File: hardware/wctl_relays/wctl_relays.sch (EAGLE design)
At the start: 38 parts, among them IC1 74LS595D

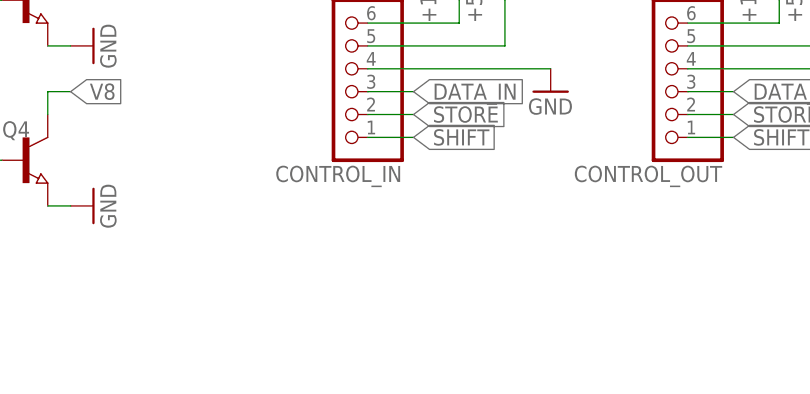
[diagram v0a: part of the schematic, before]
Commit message: Migrated back to ESP32, updated pins in code and updated hardware, also updated readme
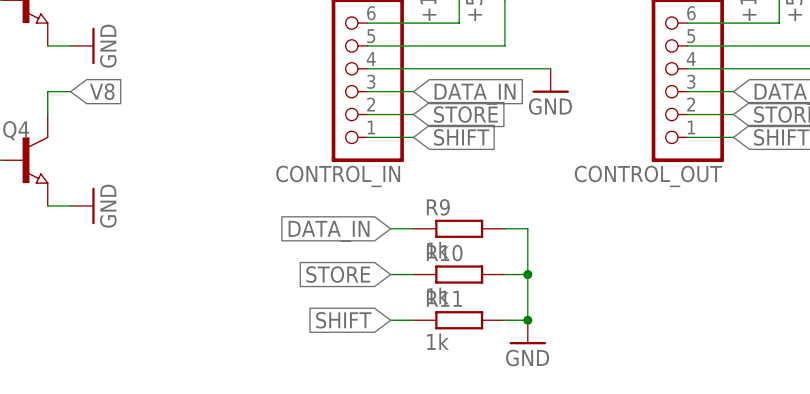
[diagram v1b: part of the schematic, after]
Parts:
- added R10, R11, R9: 1k, rcl:R-EU_R0603
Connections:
- net DATA_IN: now also R9.1
- net GND: now also R10.2, R11.2, R9.2
- net SHIFT: now also R11.1
- net STORE: now also R10.1
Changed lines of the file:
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@@
 <part name="P+6" library="supply1" library_urn="urn:adsk.eagle:library:371" deviceset="+12V" device=""/>
 <part name="P+7" library="supply1" library_urn="urn:adsk.eagle:library:371" deviceset="+5V" device=""/>
+<part name="R9" library="rcl" library_urn="urn:adsk.eagle:library:334" deviceset="R-EU_" device="R0603" package3d_urn="urn:adsk.eagle:package:23555/3" value="1k"/>
+<part name="R10" library="rcl" library_urn="urn:adsk.eagle:library:334" deviceset="R-EU_" device="R0603" package3d_urn="urn:adsk.eagle:package:23555/3" value="1k"/>
+<part name="R11" library="rcl" library_urn="urn:adsk.eagle:library:334" deviceset="R-EU_" device="R0603" package3d_urn="urn:adsk.eagle:package:23555/3" value="1k"/>
+<part name="GND13" library="supply1" library_urn="urn:adsk.eagle:library:371" deviceset="GND" device=""/>
 </parts>
 <sheets>
@@
 <instance part="P+7" gate="1" x="50.8" y="12.7" smashed="yes" grouprefs="CONTROL_IO">
 <attribute name="VALUE" x="48.26" y="7.62" size="1.778" layer="96" rot="R90"/>
+</instance>
+<instance part="R9" gate="G$1" x="10.16" y="-15.24" smashed="yes" grouprefs="CONTROL_IO">
+<attribute name="NAME" x="6.35" y="-13.7414" size="1.778" layer="95"/>
+<attribute name="VALUE" x="6.35" y="-18.542" size="1.778" layer="96"/>
+</instance>
+<instance part="R10" gate="G$1" x="10.16" y="-20.32" smashed="yes" grouprefs="CONTROL_IO">
+<attribute name="NAME" x="6.35" y="-18.8214" size="1.778" layer="95"/>
+<attribute name="VALUE" x="6.35" y="-23.622" size="1.778" layer="96"/>
+</instance>
+<instance part="R11" gate="G$1" x="10.16" y="-25.4" smashed="yes" grouprefs="CONTROL_IO">
+<attribute name="NAME" x="6.35" y="-23.9014" size="1.778" layer="95"/>
+<attribute name="VALUE" x="6.35" y="-28.702" size="1.778" layer="96"/>
+</instance>
+<instance part="GND13" gate="1" x="17.78" y="-27.94" smashed="yes" grouprefs="CONTROL_IO">
+<attribute name="VALUE" x="15.24" y="-30.48" size="1.778" layer="96"/>
 </instance>
 </instances>
@@
 <pinref part="GND12" gate="1" pin="GND"/>
 </segment>
+<segment>
+<pinref part="R9" gate="G$1" pin="2"/>
+<wire x1="15.24" y1="-15.24" x2="17.78" y2="-15.24" width="0.1524" layer="91" grouprefs="CONTROL_IO"/>
+<wire x1="17.78" y1="-15.24" x2="17.78" y2="-20.32" width="0.1524" layer="91" grouprefs="CONTROL_IO"/>
+<pinref part="R10" gate="G$1" pin="2"/>
+<wire x1="17.78" y1="-20.32" x2="15.24" y2="-20.32" width="0.1524" layer="91" grouprefs="CONTROL_IO"/>
+<pinref part="R11" gate="G$1" pin="2"/>
+<wire x1="15.24" y1="-25.4" x2="17.78" y2="-25.4" width="0.1524" layer="91" grouprefs="CONTROL_IO"/>
+<wire x1="17.78" y1="-25.4" x2="17.78" y2="-20.32" width="0.1524" layer="91" grouprefs="CONTROL_IO"/>
+<junction x="17.78" y="-20.32" grouprefs="CONTROL_IO"/>
+<pinref part="GND13" gate="1" pin="GND"/>
+<junction x="17.78" y="-25.4" grouprefs="CONTROL_IO"/>
+</segment>
 </net>
 <net name="DATA_IN" class="0">
@@
 <label x="-101.6" y="99.06" size="1.778" layer="95" rot="R180" xref="yes" grouprefs="RELAY_CONTROL"/>
 </segment>
+<segment>
+<pinref part="R9" gate="G$1" pin="1"/>
+<wire x1="5.08" y1="-15.24" x2="2.54" y2="-15.24" width="0.1524" layer="91" grouprefs="CONTROL_IO"/>
+<label x="2.54" y="-15.24" size="1.778" layer="95" rot="R180" xref="yes" grouprefs="CONTROL_IO"/>
+</segment>
 </net>
 <net name="STORE" class="0">
@@
 <label x="40.64" y="-2.54" size="1.778" layer="95" xref="yes" grouprefs="CONTROL_IO"/>
 </segment>
+<segment>
+<pinref part="R10" gate="G$1" pin="1"/>
+<wire x1="5.08" y1="-20.32" x2="2.54" y2="-20.32" width="0.1524" layer="91" grouprefs="CONTROL_IO"/>
+<label x="2.54" y="-20.32" size="1.778" layer="95" rot="R180" xref="yes" grouprefs="CONTROL_IO"/>
+</segment>
 </net>
 <net name="SHIFT" class="0">
@@
 <label x="40.64" y="-5.08" size="1.778" layer="95" xref="yes" grouprefs="CONTROL_IO"/>
 </segment>
-</net>
+<segment>
+<pinref part="R11" gate="G$1" pin="1"/>
+<wire x1="5.08" y1="-25.4" x2="2.54" y2="-25.4" width="0.1524" layer="91" grouprefs="CONTROL_IO"/>
+<label x="2.54" y="-25.4" size="1.778" layer="95" rot="R180" xref="yes" grouprefs="CONTROL_IO"/>
+</segment>
+</net>
